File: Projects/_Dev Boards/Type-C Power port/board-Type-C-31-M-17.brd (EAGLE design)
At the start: 18.5 x 23 mm, 2 parts, among them J1 USB-TYPE-C-31-M-17

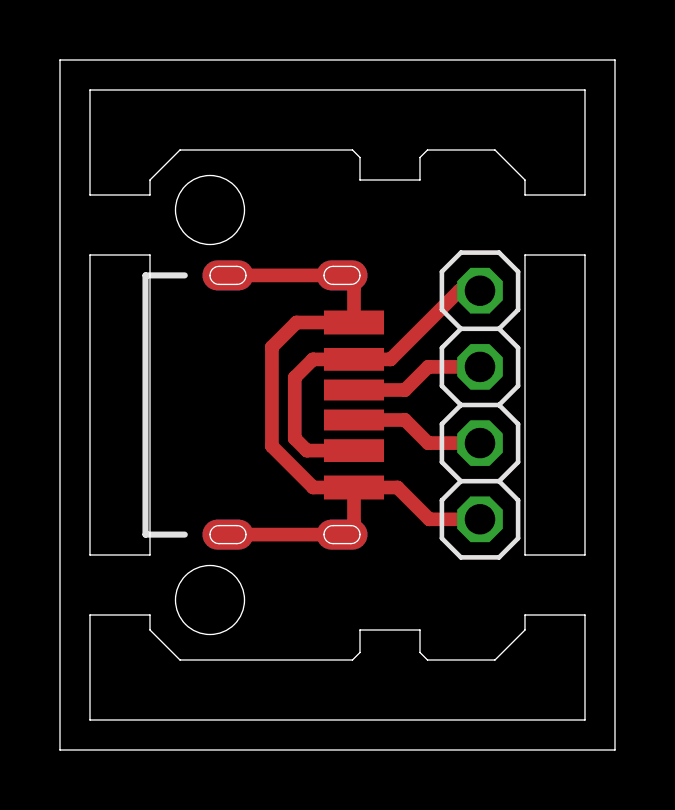
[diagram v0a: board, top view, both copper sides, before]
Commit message: updated Type-C power board
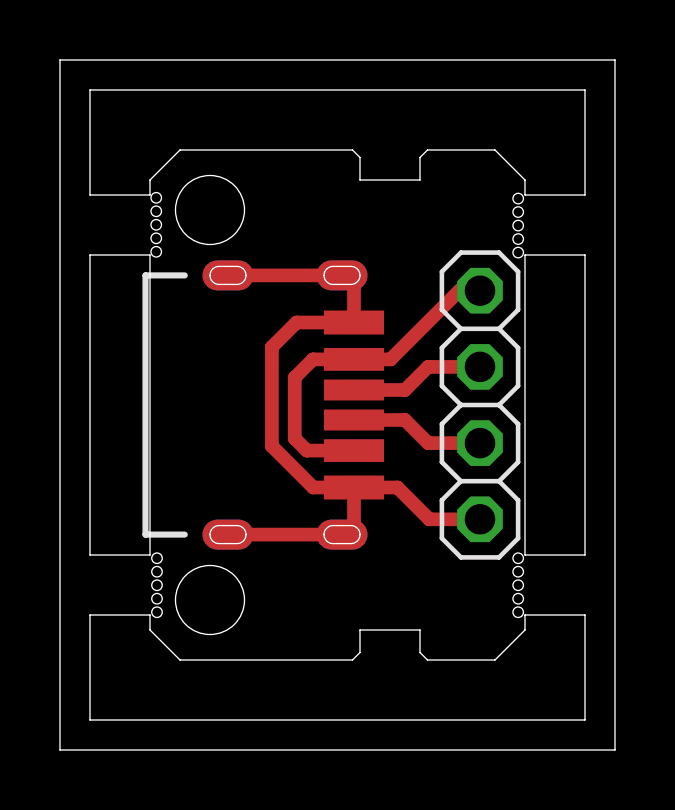
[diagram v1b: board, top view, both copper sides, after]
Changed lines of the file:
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@@
 <?xml version="1.0" encoding="utf-8"?>
 <!DOCTYPE eagle SYSTEM "eagle.dtd">
-<eagle version="9.6.0">
+<eagle version="9.6.1">
 <drawing>
 <settings>
@@
 <setting verticaltext="up"/>
 </settings>
-<grid distance="1" unitdist="mm" unit="mm" style="lines" multiple="1" display="yes" altdistance="5" altunitdist="mil" altunit="mil"/>
+<grid distance="1" unitdist="mil" unit="mil" style="lines" multiple="1" display="yes" altdistance="5" altunitdist="mil" altunit="mil"/>
 <layers>
 <layer number="1" name="Top" color="4" fill="1" visible="yes" active="yes"/>
@@
 <layer number="20" name="Dimension" color="24" fill="1" visible="yes" active="yes"/>
 <layer number="21" name="tPlace" color="7" fill="1" visible="yes" active="yes"/>
-<layer number="22" name="bPlace" color="7" fill="1" visible="no" active="yes"/>
+<layer number="22" name="bPlace" color="7" fill="1" visible="yes" active="yes"/>
 <layer number="23" name="tOrigins" color="15" fill="1" visible="yes" active="yes"/>
 <layer number="24" name="bOrigins" color="15" fill="1" visible="yes" active="yes"/>
-<layer number="25" name="tNames" color="7" fill="1" visible="no" active="yes"/>
-<layer number="26" name="bNames" color="7" fill="1" visible="no" active="yes"/>
+<layer number="25" name="tNames" color="7" fill="1" visible="yes" active="yes"/>
+<layer number="26" name="bNames" color="7" fill="1" visible="yes" active="yes"/>
 <layer number="27" name="tValues" color="7" fill="1" visible="no" active="yes"/>
 <layer number="28" name="bValues" color="7" fill="1" visible="no" active="yes"/>
@@
 <layer number="43" name="vRestrict" color="2" fill="10" visible="no" active="yes"/>
 <layer number="44" name="Drills" color="7" fill="1" visible="no" active="yes"/>
-<layer number="45" name="Holes" color="7" fill="1" visible="yes" active="yes"/>
+<layer number="45" name="Holes" color="7" fill="1" visible="no" active="yes"/>
 <layer number="46" name="Milling" color="3" fill="1" visible="no" active="yes"/>
 <layer number="47" name="Measures" color="7" fill="1" visible="no" active="yes"/>
@@
 <hole x="2" y="15" drill="2.3"/>
 <hole x="2" y="2" drill="2.3"/>
-<dimension x1="0" y1="1" x2="12.5" y2="1" x3="6.25" y3="1" textsize="1.27" textratio="12" layer="21" width="0.08"/>
-<dimension x1="4.75" y1="0" x2="4.75" y2="17" x3="4.008" y3="8.5" textsize="1.27" textratio="12" layer="21" dtype="vertical" width="0.08"/>
-<dimension x1="0.85" y1="15" x2="3.15" y2="15" x3="2" y3="14.2" textsize="1.27" textratio="12" layer="21" width="0.08" extlength="0.5"/>
 <wire x1="0" y1="1" x2="7" y2="1" width="0.08" layer="22"/>
 <wire x1="9" y1="1" x2="12.5" y2="1" width="0.08" layer="22"/>
@@
 <wire x1="6.7" y1="17" x2="6.7" y2="16" width="0.08" layer="22"/>
 <text x="6.5" y="15.8" size="1.016" layer="22" font="vector" ratio="12" rot="MR0">1.0</text>
-<text x="12.06" y="13.63" size="1.27" layer="22" font="vector" ratio="15" rot="MR0">VBUS</text>
-<text x="9.41" y="10.16" size="1.27" layer="22" font="vector" ratio="12" rot="MR270" align="center">CC1</text>
-<text x="9.45" y="6.66" size="1.27" layer="22" font="vector" ratio="12" rot="MR270" align="center">CC2</text>
-<text x="12.06" y="2.51" size="1.27" layer="22" font="vector" ratio="15" rot="MR0">GND</text>
+<text x="8.9" y="13.9" size="1.27" layer="22" font="vector" ratio="15" rot="MR270" align="center">VBUS</text>
+<text x="8.9" y="10.16" size="1.27" layer="22" font="vector" ratio="12" rot="MR270" align="center">CC1</text>
+<text x="8.9" y="7.16" size="1.27" layer="22" font="vector" ratio="12" rot="MR270" align="center">CC2</text>
+<text x="8.9" y="3.9" size="1.27" layer="22" font="vector" ratio="15" rot="MR270" align="center">GND</text>
 <wire x1="0" y1="1" x2="0" y2="1.5" width="0" layer="20"/>
 <wire x1="0" y1="3.5" x2="0" y2="13.5" width="0" layer="20"/>
@@
 <wire x1="15.5" y1="20" x2="-3" y2="20" width="0" layer="20"/>
 <wire x1="-3" y1="20" x2="-3" y2="-3" width="0" layer="20"/>
+<hole x="0.208" y="15.4066" drill="0.35"/>
+<hole x="0.208" y="14.9566" drill="0.35"/>
+<hole x="0.208" y="14.5066" drill="0.35"/>
+<hole x="0.208" y="14.0566" drill="0.35"/>
+<hole x="0.208" y="13.6066" drill="0.35"/>
+<hole x="12.273" y="15.3812" drill="0.35"/>
+<hole x="12.273" y="14.9312" drill="0.35"/>
+<hole x="12.273" y="14.4812" drill="0.35"/>
+<hole x="12.273" y="14.0312" drill="0.35"/>
+<hole x="12.273" y="13.5812" drill="0.35"/>
+<hole x="12.273" y="3.3924" drill="0.35"/>
+<hole x="12.273" y="2.9424" drill="0.35"/>
+<hole x="12.273" y="2.4924" drill="0.35"/>
+<hole x="12.273" y="2.0424" drill="0.35"/>
+<hole x="12.273" y="1.5924" drill="0.35"/>
+<hole x="0.2334" y="3.3924" drill="0.35"/>
+<hole x="0.2334" y="2.9424" drill="0.35"/>
+<hole x="0.2334" y="2.4924" drill="0.35"/>
+<hole x="0.2334" y="2.0424" drill="0.35"/>
+<hole x="0.2334" y="1.5924" drill="0.35"/>
 </plain>
 <attributes>
@@
 </class>
 </classes>
-<designrules name="default *">
+<designrules name="JLCPCB_2-Layer">
 <description language="de">&lt;b&gt;EAGLE Design Rules&lt;/b&gt;
 &lt;p&gt;
@@
 Einstellungen hier und speichern die Design Rules unter
 einem neuen Namen ab.</description>
-<description language="en">&lt;b&gt;EAGLE Design Rules&lt;/b&gt;
+<description language="en">&lt;b&gt;JLCPCB 2-layer PCB Design Rules&lt;/b&gt;
 &lt;p&gt;
-The default Design Rules have been set to cover
-a wide range of applications. Your particular design
-may have different requirements, so please make the
-necessary adjustments and save your customized
-design rules under a new name.</description>
+Source: &lt;a href=&quot;https://jlcpcb.com/capabilities/Capabilities&quot;&gt;JLCPCB specs&lt;/a&gt;
+&lt;/p&gt;</description>
 <param name="layerSetup" value="(1*16)"/>
 <param name="mtCopper" value="0.035mm 0.035mm 0.035mm 0.035mm 0.035mm 0.035mm 0.035mm 0.035mm 0.035mm 0.035mm 0.035mm 0.035mm 0.035mm 0.035mm 0.035mm 0.035mm"/>
 <param name="mtIsolate" value="1.5mm 0.15mm 0.2mm 0.15mm 0.2mm 0.15mm 0.2mm 0.15mm 0.2mm 0.15mm 0.2mm 0.15mm 0.2mm 0.15mm 0.2mm"/>
-<param name="mdWireWire" value="6mil"/>
-<param name="mdWirePad" value="6mil"/>
-<param name="mdWireVia" value="6mil"/>
-<param name="mdPadPad" value="6mil"/>
-<param name="mdPadVia" value="6mil"/>
-<param name="mdViaVia" value="6mil"/>
-<param name="mdSmdPad" value="6mil"/>
-<param name="mdSmdVia" value="6mil"/>
-<param name="mdSmdSmd" value="6mil"/>
+<param name="mdWireWire" value="5mil"/>
+<param name="mdWirePad" value="5mil"/>
+<param name="mdWireVia" value="5mil"/>
+<param name="mdPadPad" value="5mil"/>
+<param name="mdPadVia" value="5mil"/>
+<param name="mdViaVia" value="5mil"/>
+<param name="mdSmdPad" value="5mil"/>
+<param name="mdSmdVia" value="5mil"/>
+<param name="mdSmdSmd" value="5mil"/>
 <param name="mdViaViaSameLayer" value="6mil"/>
 <param name="mnLayersViaInSmd" value="2"/>
-<param name="mdCopperDimension" value="4mil"/>
-<param name="mdDrill" value="6mil"/>
+<param name="mdCopperDimension" value="8mil"/>
+<param name="mdDrill" value="3mil"/>
 <param name="mdSmdStop" value="0mil"/>
-<param name="msWidth" value="6mil"/>
-<param name="msDrill" value="0.35mm"/>
+<param name="msWidth" value="5mil"/>
+<param name="msDrill" value="0.2mm"/>
 <param name="msMicroVia" value="9.99mm"/>
 <param name="msBlindViaRatio" value="0.5"/>
@@
 <param name="rvMicroViaOuter" value="0.25"/>
 <param name="rvMicroViaInner" value="0.25"/>
-<param name="rlMinPadTop" value="10mil"/>
+<param name="rlMinPadTop" value="3mil"/>
 <param name="rlMaxPadTop" value="20mil"/>
-<param name="rlMinPadInner" value="10mil"/>
+<param name="rlMinPadInner" value="3mil"/>
 <param name="rlMaxPadInner" value="20mil"/>
-<param name="rlMinPadBottom" value="10mil"/>
+<param name="rlMinPadBottom" value="3mil"/>
 <param name="rlMaxPadBottom" value="20mil"/>
-<param name="rlMinViaOuter" value="8mil"/>
+<param name="rlMinViaOuter" value="0.2mm"/>
 <param name="rlMaxViaOuter" value="20mil"/>
-<param name="rlMinViaInner" value="8mil"/>
+<param name="rlMinViaInner" value="0.2mm"/>
 <param name="rlMaxViaInner" value="20mil"/>
 <param name="rlMinMicroViaOuter" value="4mil"/>
@@
 <param name="mlMinCreamFrame" value="0mil"/>
 <param name="mlMaxCreamFrame" value="0mil"/>
-<param name="mlViaStopLimit" value="0mil"/>
+<param name="mlViaStopLimit" value="15mil"/>
 <param name="srRoundness" value="0"/>
-<param name="srMinRoundness" value="0mil"/>
+<param name="srMinRoundness" value="1mil"/>
 <param name="srMaxRoundness" value="0mil"/>
-<param name="slThermalIsolate" value="10mil"/>
+<param name="slThermalIsolate" value="8mil"/>
 <param name="slThermalsForVias" value="0"/>
 <param name="dpMaxLengthDifference" value="10mm"/>

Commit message: update
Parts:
- added R1, R2: 5.1k, angrypig7-RCL:R0603
- JP1: device pinhead_v2:1X04/OCT -> angrypig7-Connectors-PinHeads:1X04
- moved J1 0.20 mm to (6.60, 8.50)
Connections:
- removed net N$3: J1.CC1, JP1.2
- removed net N$4: J1.CC2, JP1.3
- new net GND: J1.GND, J1.GND_2, J1.SHLD-B1, J1.SHLD-B2, J1.SHLD-B3, J1.SHLD-B4, J1.SHLD-T1, J1.SHLD-T2, J1.SHLD-T3, J1.SHLD-T4, JP1.3, JP1.4, R1.2, R2.2
- new net VBUS: J1.VBUS, J1.VBUS_2, JP1.1, JP1.2
- net N$1: now also J1.CC1, R1.1; no longer J1.GND, J1.GND_2, J1.SHLD-B1, J1.SHLD-B2, J1.SHLD-B3, J1.SHLD-B4, J1.SHLD-T1, J1.SHLD-T2, J1.SHLD-T3, J1.SHLD-T4, JP1.4
- net N$2: now also J1.CC2, R2.1; no longer J1.VBUS, J1.VBUS_2, JP1.1
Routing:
- net N$1: track 25.4 -> 3.01 mm, vias 0 -> 1
- net VBUS: track 0.00 -> 11.2 mm
- net N$2: track 11.5 -> 3.01 mm, vias 0 -> 1
- net N$4: track 4.52 -> 0.00 mm
- net N$3: track 4.52 -> 0.00 mm
- added copper zone on layer 1, net GND
- added copper zone on layer 16, net GND
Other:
- board text removed: "CC1"
- board text removed: "CC2"
